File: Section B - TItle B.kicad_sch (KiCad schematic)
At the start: 11 parts, among them Q1 CSD18534Q5A, Q3 BSS123, Q4 BSS84, Q5 BSS123

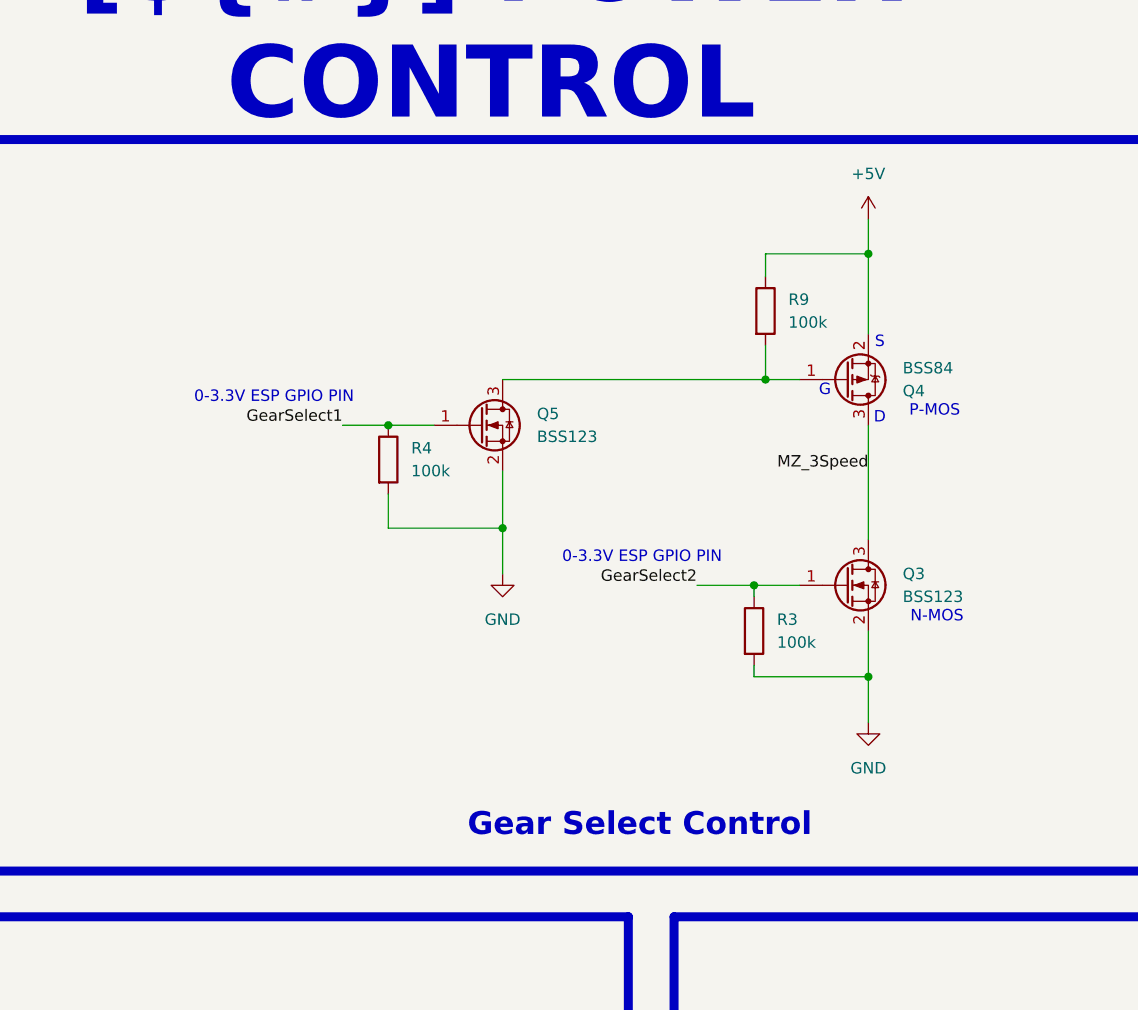
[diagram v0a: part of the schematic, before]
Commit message: [SCHEMATICS] Ajout de convertisseur + autres
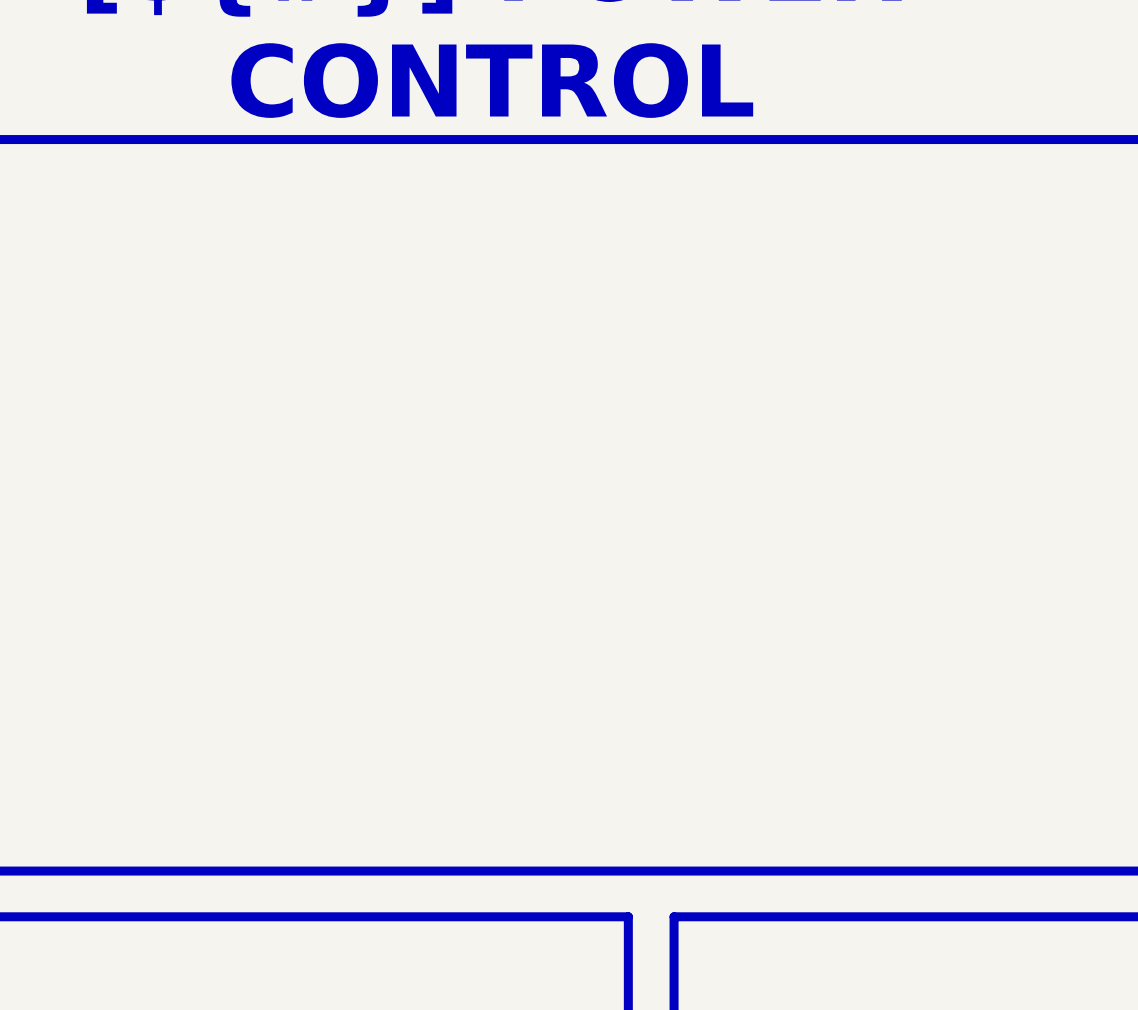
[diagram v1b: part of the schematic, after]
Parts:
- removed Q3, Q5: BSS123, Package_TO_SOT_SMD:SOT-23, symbol Transistor_FET:BSS123
- removed Q4: BSS84, Package_TO_SOT_SMD:SOT-23, symbol Transistor_FET:BSS84
- removed R3, R4, R9: 100k, Resistor_SMD:R_0603_1608Metric_Pad0.98x0.95mm_HandSolder, symbol Device:R
- D1: Manufacturer Part Number (none) -> BZT52C3V3
- Q1: Manufacturer Part Number (none) -> CBG322513U601T
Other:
- note removed: "0-3.3V ESP GPIO PIN"
- note removed: "D"
- note removed: "G"
- note removed: "N-MOS"
- note removed: "P-MOS"
- note removed: "S"
